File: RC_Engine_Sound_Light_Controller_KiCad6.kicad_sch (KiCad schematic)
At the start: 36 parts, among them J1 RX, J10 RGB, J11 32, J12 CH1, J13 CH2, J14 CH3, J15 ESC, J16 CH4, J2 HeadL, J3 TailL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

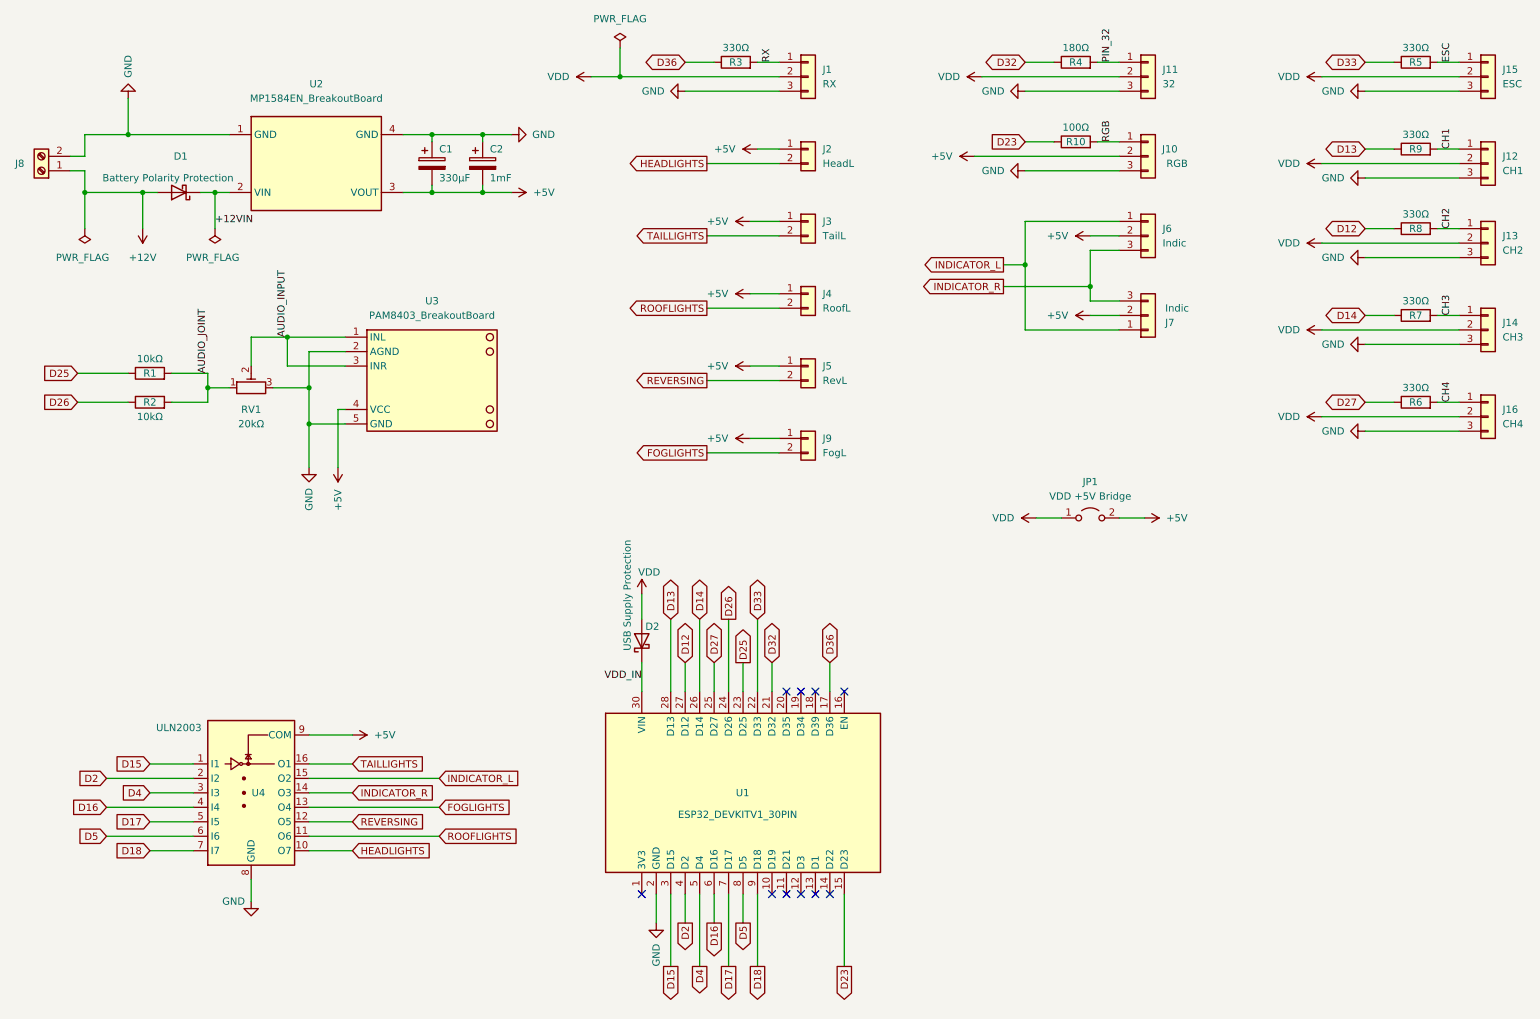
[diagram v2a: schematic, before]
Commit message: Changed +5V to VCC.
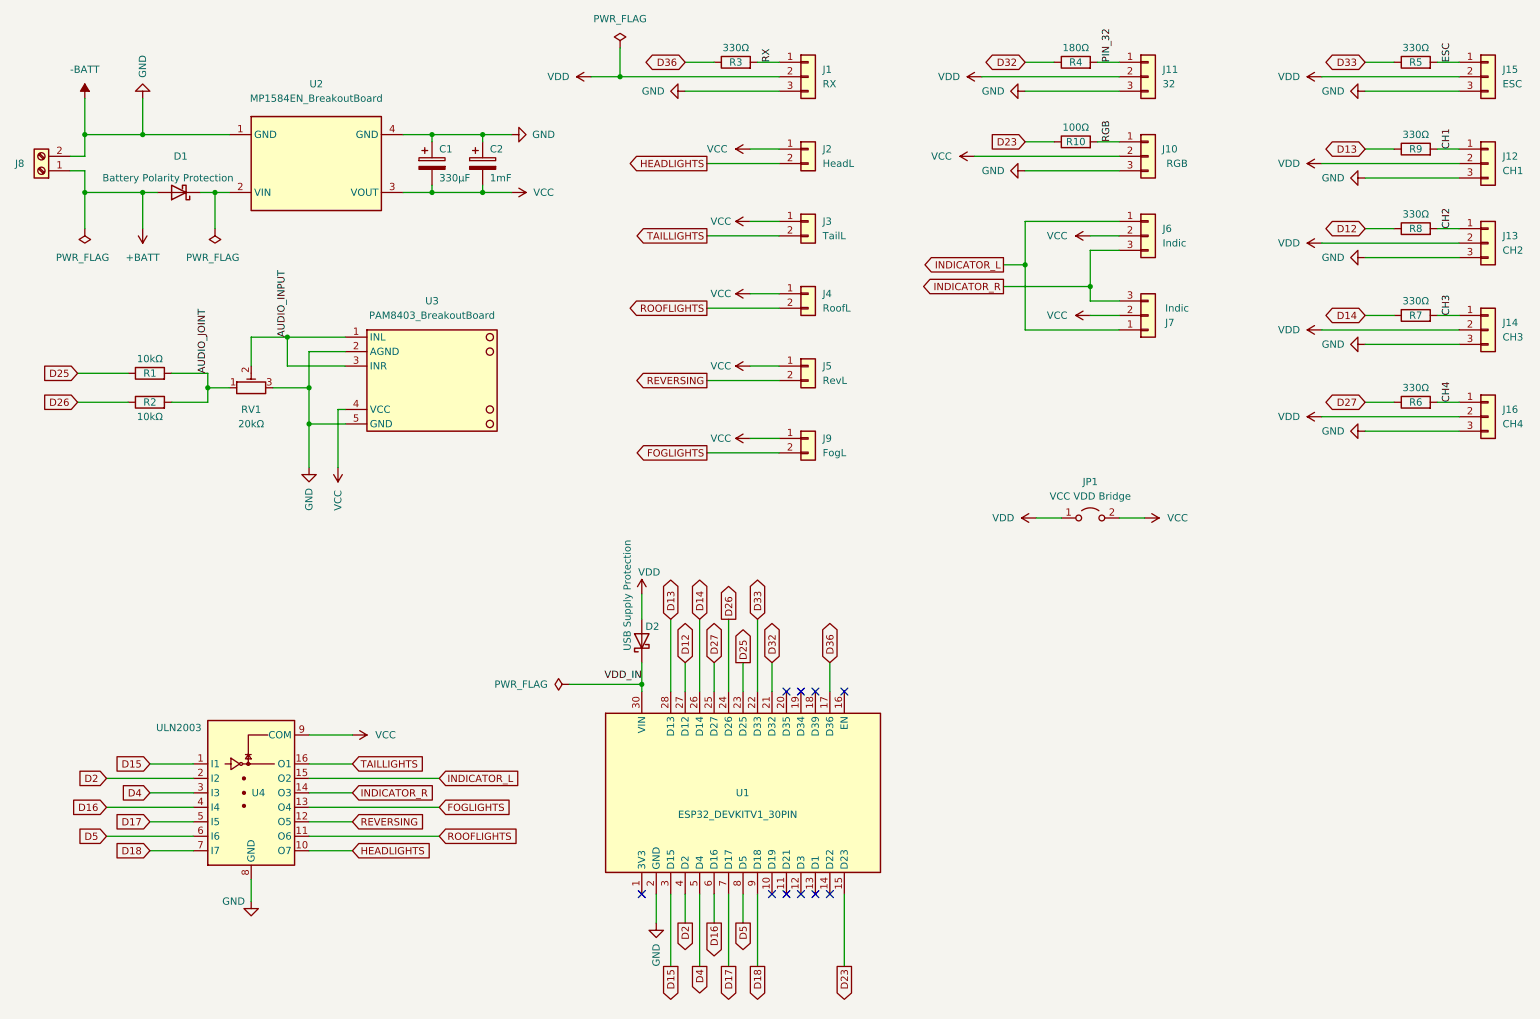
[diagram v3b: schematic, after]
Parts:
- JP1: value VDD +5V Bridge -> VCC VDD Bridge
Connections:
- net +12V renamed +BATT
- net +12VIN: no longer names the net of D1.1 (K), U2.2 (VIN), U2.6 (VIN)
- net +5V renamed VCC
- net GND renamed -BATT

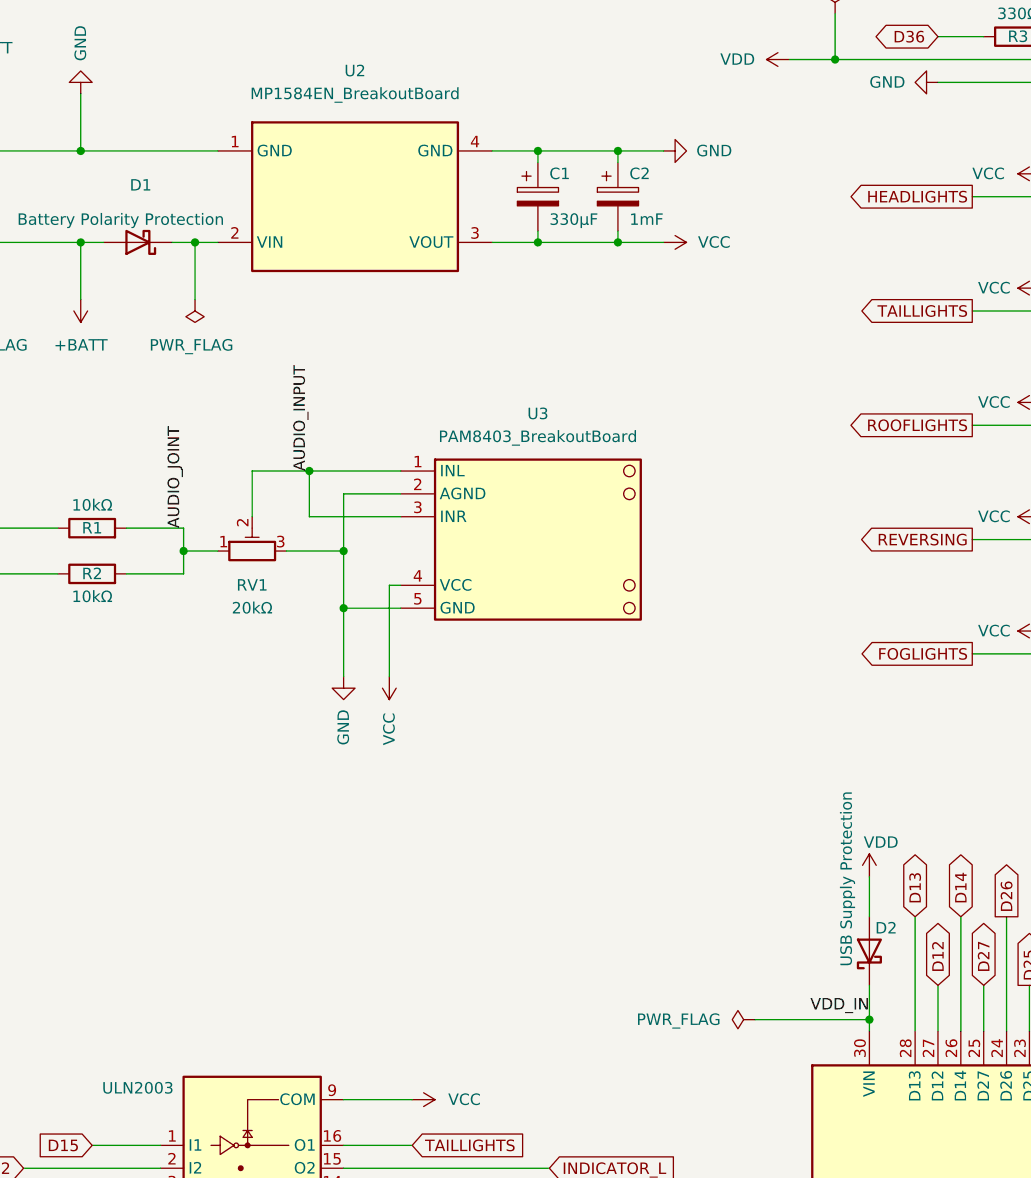
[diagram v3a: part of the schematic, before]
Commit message: Corrected 5V caps silkscreen polarization.
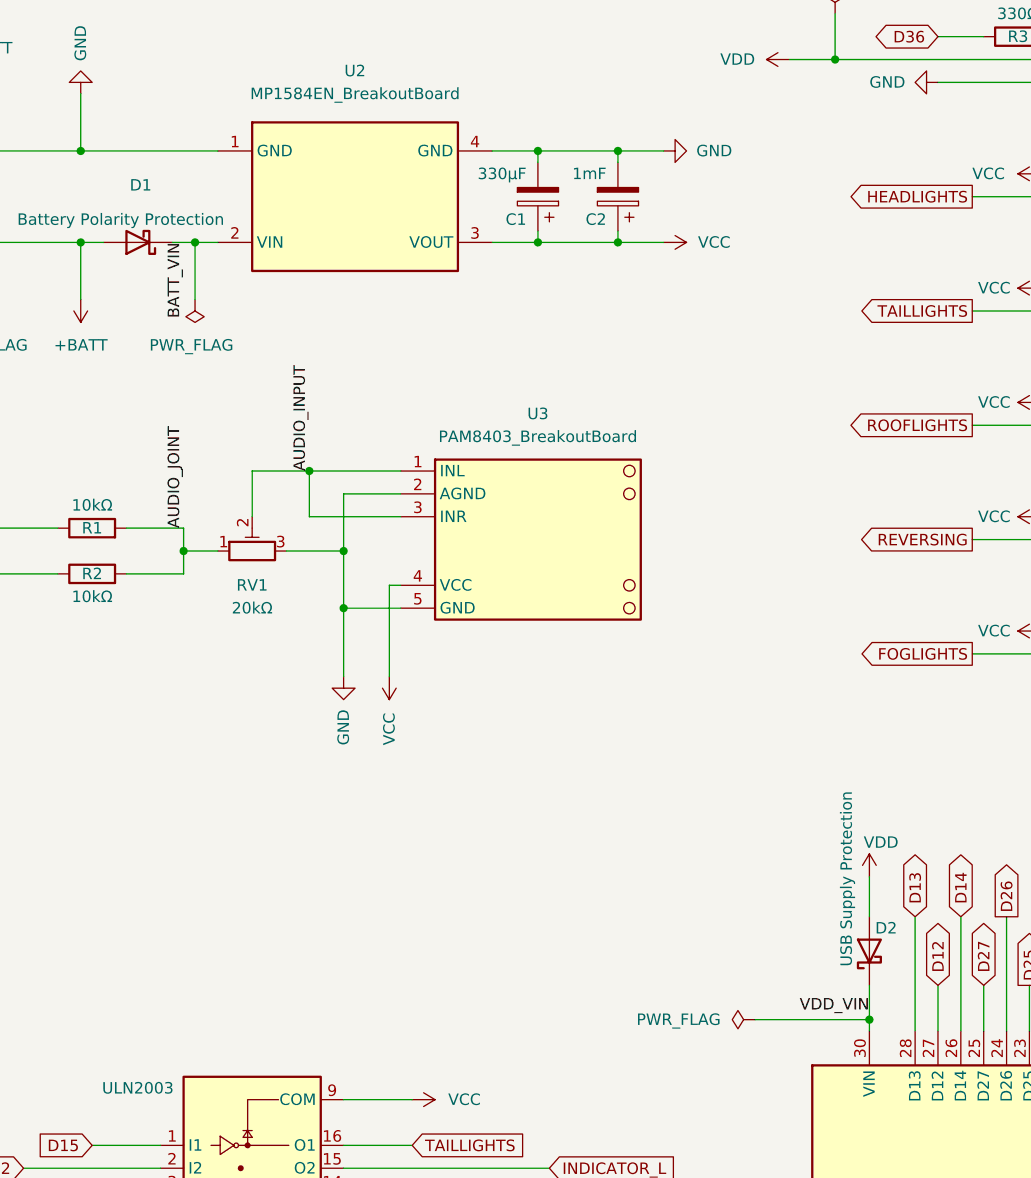
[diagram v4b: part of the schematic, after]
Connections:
- net -BATT: now also C1.2, C2.2; no longer C1.1, C2.1
- net VCC: now also C1.1, C2.1; no longer C1.2, C2.2
- net BATT_VIN: now reaches D1.1 (K), U2.2 (VIN), U2.6 (VIN)
- net VDD_IN renamed VDD_VIN
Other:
- moved on the sheet: C1, C2
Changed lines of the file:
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@@
     (stroke (width 0) (type default) (color 0 0 0 0))
   )
-  (label "VDD_IN" (at 124.46 131.445 180)
+  (label "VDD_VIN" (at 124.46 131.445 180)
     (effects (font (size 1.27 1.27)) (justify right bottom))
   )
   (label "CH3" (at 266.7 67.31 90)
     (effects (font (size 1.27 1.27)) (justify left bottom))
+  )
+  (label "BATT_VIN" (at 48.26 45.72 270)
+    (effects (font (size 1.27 1.27)) (justify right bottom))
   )
   (label "RX" (at 147.32 22.86 90)
@@
     (pin "2")
   )
-  (symbol (lib_id "Device:C_Polarized") (at 87.63 40.64 0) (unit 1)
-    (in_bom yes) (on_board yes)
-    (property "Reference" "C1" (id 0) (at 88.9 38.1 0)
-      (effects (font (size 1.27 1.27)) (justify left))
-    )
-    (property "Value" "330µF" (id 1) (at 88.9 43.18 0)
-      (effects (font (size 1.27 1.27)) (justify left))
-    )
-    (property "Footprint" "Capacitor_Tantalum_SMD:CP_EIA-7343-30_AVX-N_Pad2.25x2.55mm_HandSolder" (id 2) (at 88.5952 44.45 0)
+  (symbol (lib_id "Device:C_Polarized") (at 87.63 40.64 180) (unit 1)
+    (in_bom yes) (on_board yes)
+    (property "Reference" "C1" (id 0) (at 86.36 43.18 0)
+      (effects (font (size 1.27 1.27)) (justify left))
+    )
+    (property "Value" "330µF" (id 1) (at 86.36 38.1 0)
+      (effects (font (size 1.27 1.27)) (justify left))
+    )
+    (property "Footprint" "Capacitor_Tantalum_SMD:CP_EIA-7343-30_AVX-N_Pad2.25x2.55mm_HandSolder" (id 2) (at 86.6648 36.83 0)
       (effects (font (size 1.27 1.27)) hide)
     )
@@
     (pin "3")
   )
-  (symbol (lib_id "Device:C_Polarized") (at 96.52 40.64 0) (unit 1)
-    (in_bom yes) (on_board yes)
-    (property "Reference" "C2" (id 0) (at 97.79 38.1 0)
-      (effects (font (size 1.27 1.27)) (justify left))
-    )
-    (property "Value" "1mF" (id 1) (at 97.79 43.18 0)
-      (effects (font (size 1.27 1.27)) (justify left))
-    )
-    (property "Footprint" "Capacitor_THT:CP_Radial_D10.0mm_P2.50mm_P5.00mm" (id 2) (at 97.4852 44.45 0)
-      (effects (font (size 1.27 1.27)) hide)
-    )
+  (symbol (lib_id "Device:C_Polarized") (at 96.52 40.64 180) (unit 1)
+    (in_bom yes) (on_board yes)
+    (property "Reference" "C2" (id 0) (at 95.25 43.18 0)
+      (effects (font (size 1.27 1.27)) (justify left))
+    )
+    (property "Value" "1mF" (id 1) (at 95.25 38.1 0)
+      (effects (font (size 1.27 1.27)) (justify left))
+    )
+    (property "Footprint" "Capacitor_THT:CP_Radial_D10.0mm_P2.50mm_P5.00mm" (id 2) (at 95.5548 36.83 0)
+      (effects (font (size 1.27 1.27)) hide)
+    )

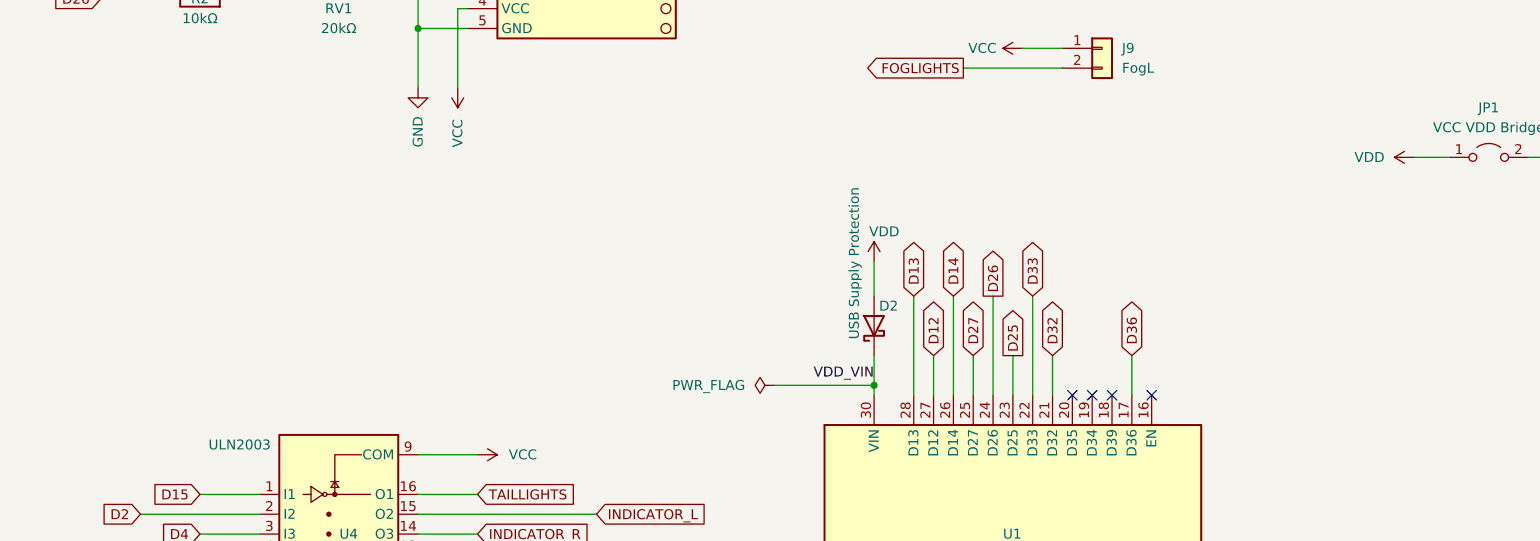
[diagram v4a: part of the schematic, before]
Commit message: Added battery voltage measurement divider, cap and (re-added) EN cap on the backside (optional).
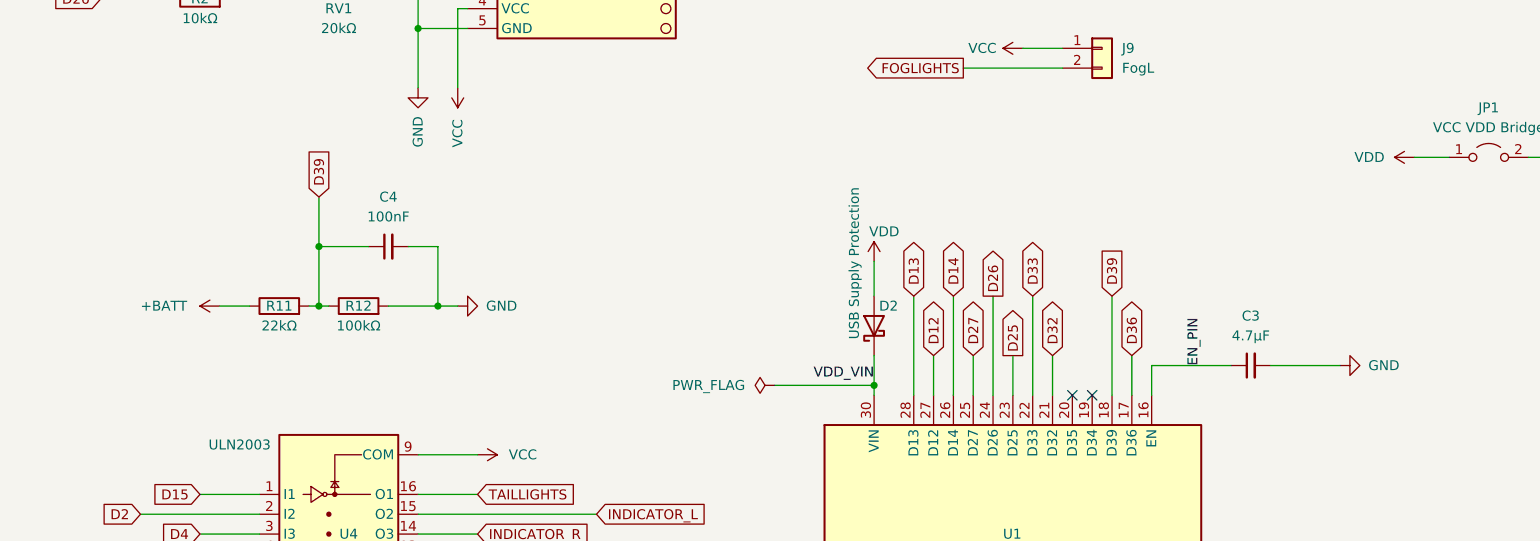
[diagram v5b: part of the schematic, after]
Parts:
- added C3: 4.7µF, Capacitor_SMD:C_1206_3216Metric_Pad1.33x1.80mm_HandSolder, symbol Device:C_Small
- added C4: 100nF, Capacitor_SMD:C_1206_3216Metric_Pad1.33x1.80mm_HandSolder, symbol Device:C_Small
- added R11: 22kΩ, Resistor_SMD:R_0805_2012Metric_Pad1.20x1.40mm_HandSolder, symbol Device:R
- added R12: 100kΩ, Resistor_SMD:R_0805_2012Metric_Pad1.20x1.40mm_HandSolder, symbol Device:R
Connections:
- net +BATT: now also R11.1
- net -BATT: now also C3.2, C4.2, R12.2
- net EN_PIN: now reaches U1.16 (EN)
- net EN_PIN: now also C3.1
- net D39: now reaches U1.18 (D39)
- net D39: now also C4.1, R11.2, R12.1
- no-connect marks 10 -> 8
